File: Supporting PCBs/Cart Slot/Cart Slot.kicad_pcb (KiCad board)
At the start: 2 copper layers, 50.4 x 21.3 mm, 4 parts, among them P1 72-Pin Connector, P2 72-Pin Connector

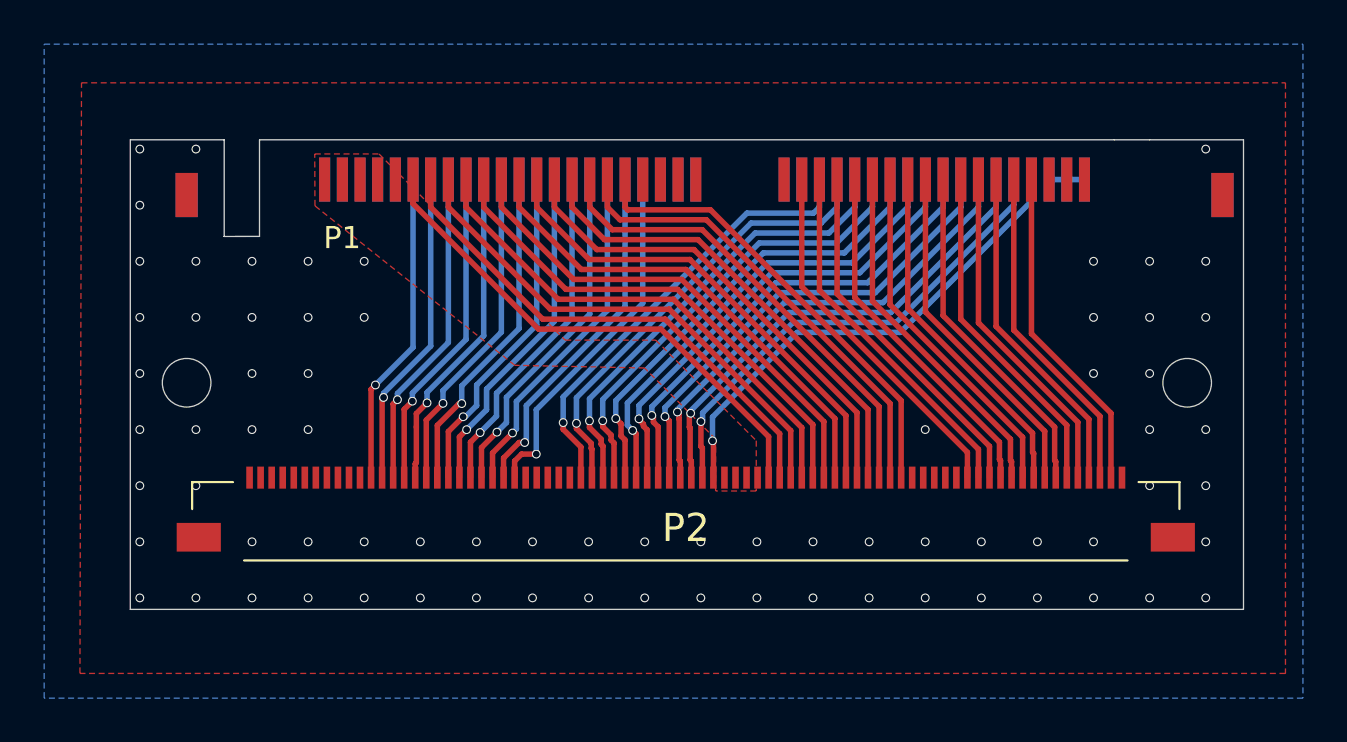
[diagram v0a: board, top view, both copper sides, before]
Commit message: + Motherboard is now V1.0 + Redesigned ScreenReg for improved reliability + Added both versions of ChargeBoost + Remove now redundant files/directories
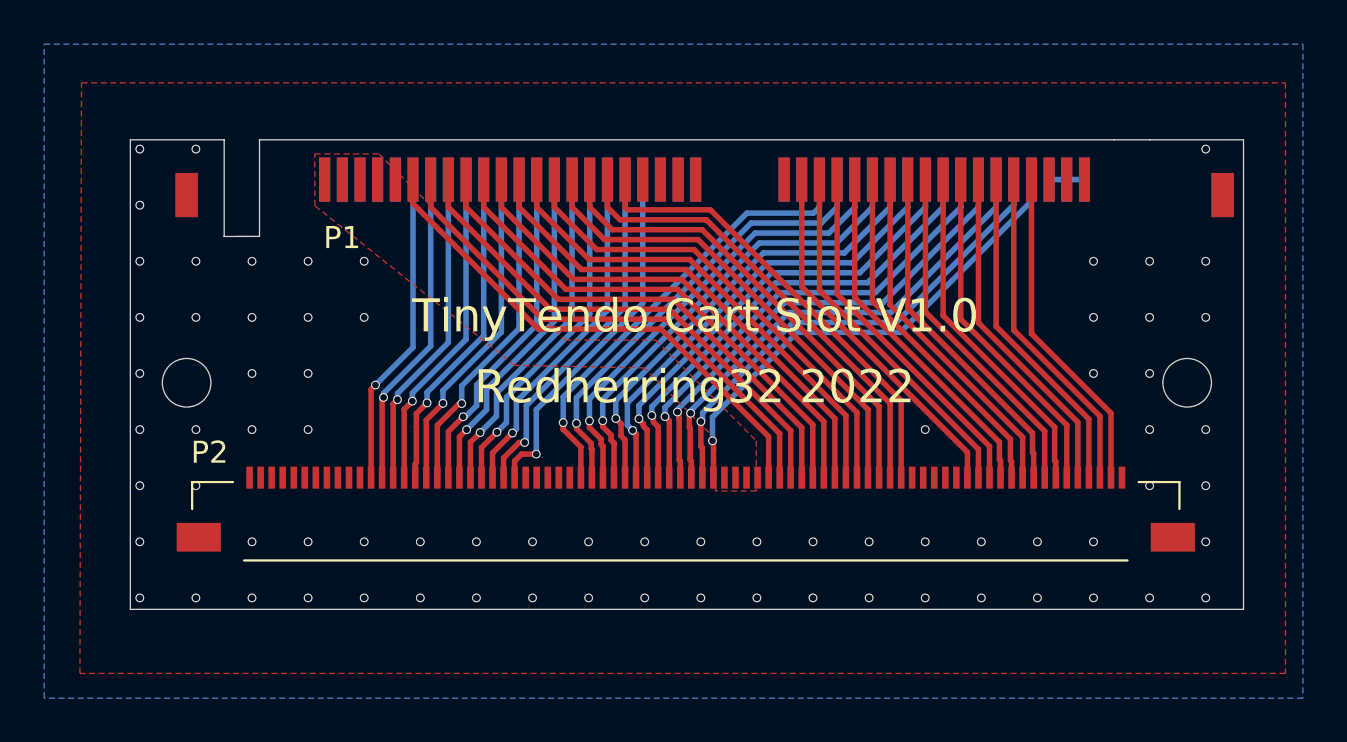
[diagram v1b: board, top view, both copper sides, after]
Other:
- board text added: "Redherring32 2022"
- board text added: "TinyTendo Cart Slot V1.0"
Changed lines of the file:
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@@
-(kicad_pcb (version 20171130) (host pcbnew "(5.1.2)-2")
+(kicad_pcb (version 20171130) (host pcbnew "(5.1.10)-1")
   (general
     (thickness 1.6)
-    (drawings 11)
+    (drawings 13)
     (tracks 419)
     (zones 0)
@@
       (drillshape 0)
       (scaleselection 1)
-      (outputdirectory "../Gerbers/"))
+      (outputdirectory "../../Extract for gerbers/"))
   )
   (net 0 "")
@@
     (tags Connector)
     (attr smd)
-    (fp_text reference P2 (at 0 -0.15) (layer F.SilkS)
-      (effects (font (size 1.27 1.27) (thickness 0.254)))
+    (fp_text reference P2 (at -21.56 -3.56) (layer F.SilkS)
+      (effects (font (size 1 1) (thickness 0.15)))
     )
     (fp_text value "72-Pin Connector" (at 0 -0.15) (layer F.SilkS) hide
@@
     )
   )
+  (gr_text "Redherring32 2022\n" (at 23 11.19) (layer F.SilkS)
+    (effects (font (size 1.5 1.5) (thickness 0.3)))
+  )
+  (gr_text "TinyTendo Cart Slot V1.0" (at 23.04 7.98) (layer F.SilkS)
+    (effects (font (size 1.5 1.5) (thickness 0.3)))
+  )
   (gr_line (start 42 0) (end 43.6 0) (layer Edge.Cuts) (width 0.05))
